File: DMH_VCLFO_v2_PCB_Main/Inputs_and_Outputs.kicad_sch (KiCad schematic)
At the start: 33 parts, among them J1 TS_Jack_6.35mm_Sw, J19 Conn_01x08, J2 TS_Jack_6.35mm_Sw, J200 IDC_02x05, J3 TS_Jack_6.35mm_Sw, J4 TS_Jack_6.35mm_Sw, J5 TS_Jack_6.35mm_Sw, J6 TS_Jack_6.35mm_Sw, J7 Conn_01x08, J8 Conn_01x08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

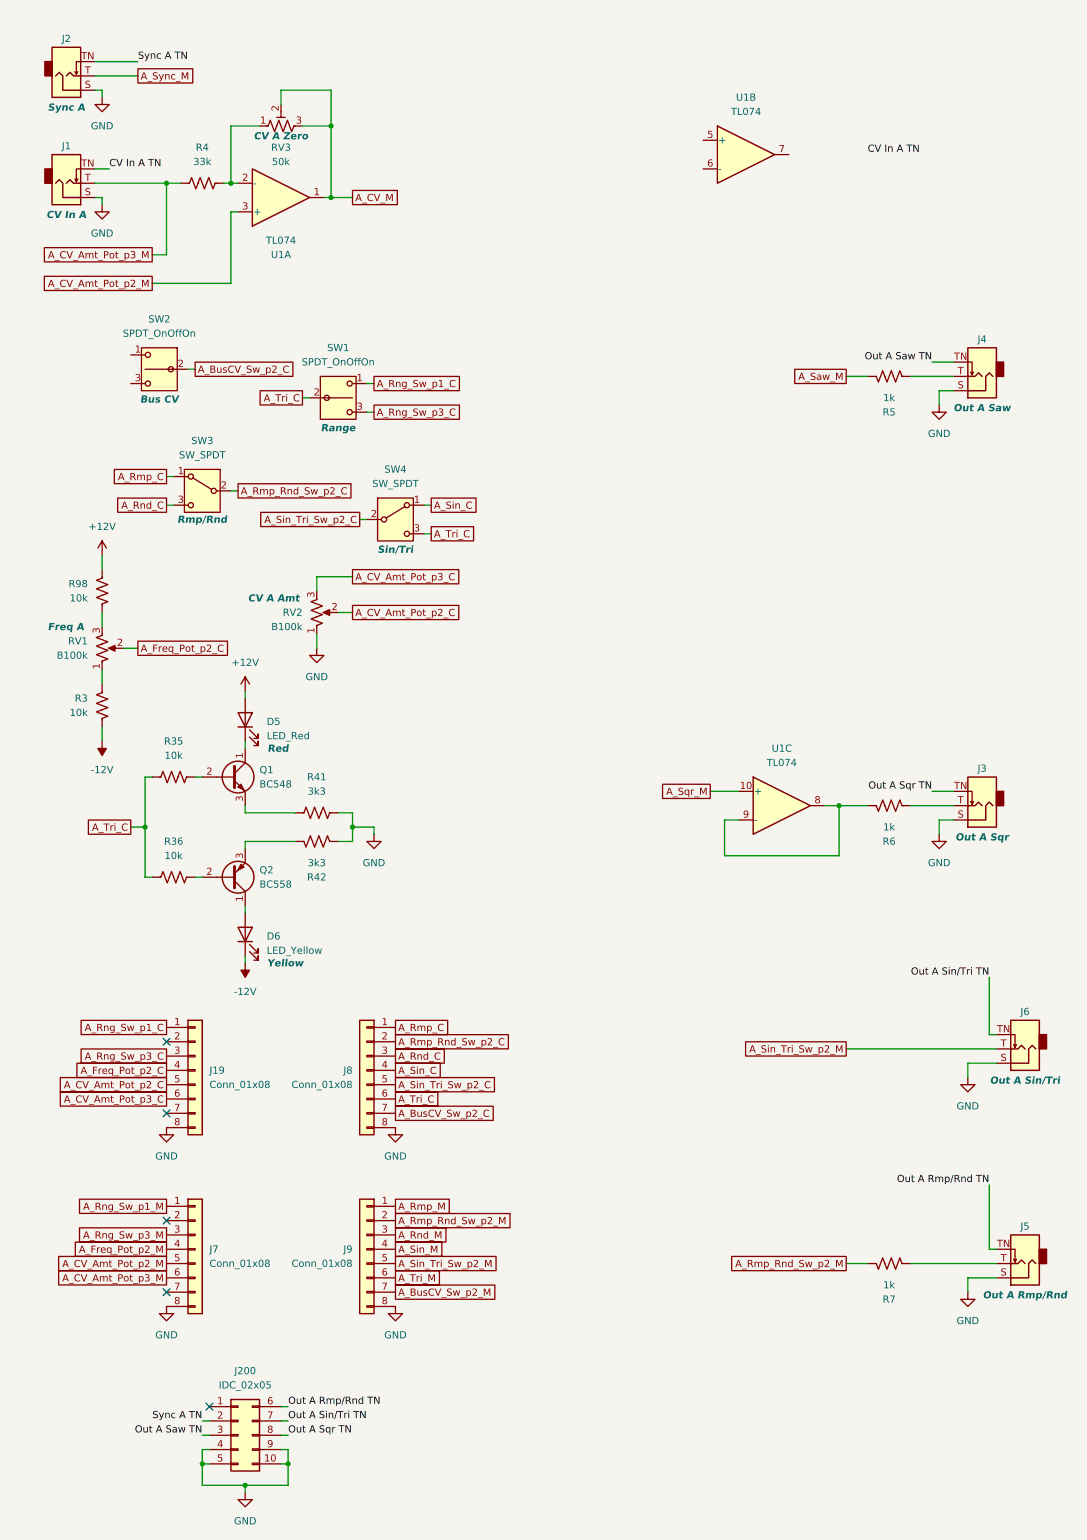
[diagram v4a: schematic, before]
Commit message: Redesigned schematic for V/Oct
And also Bus CV and Fine tune
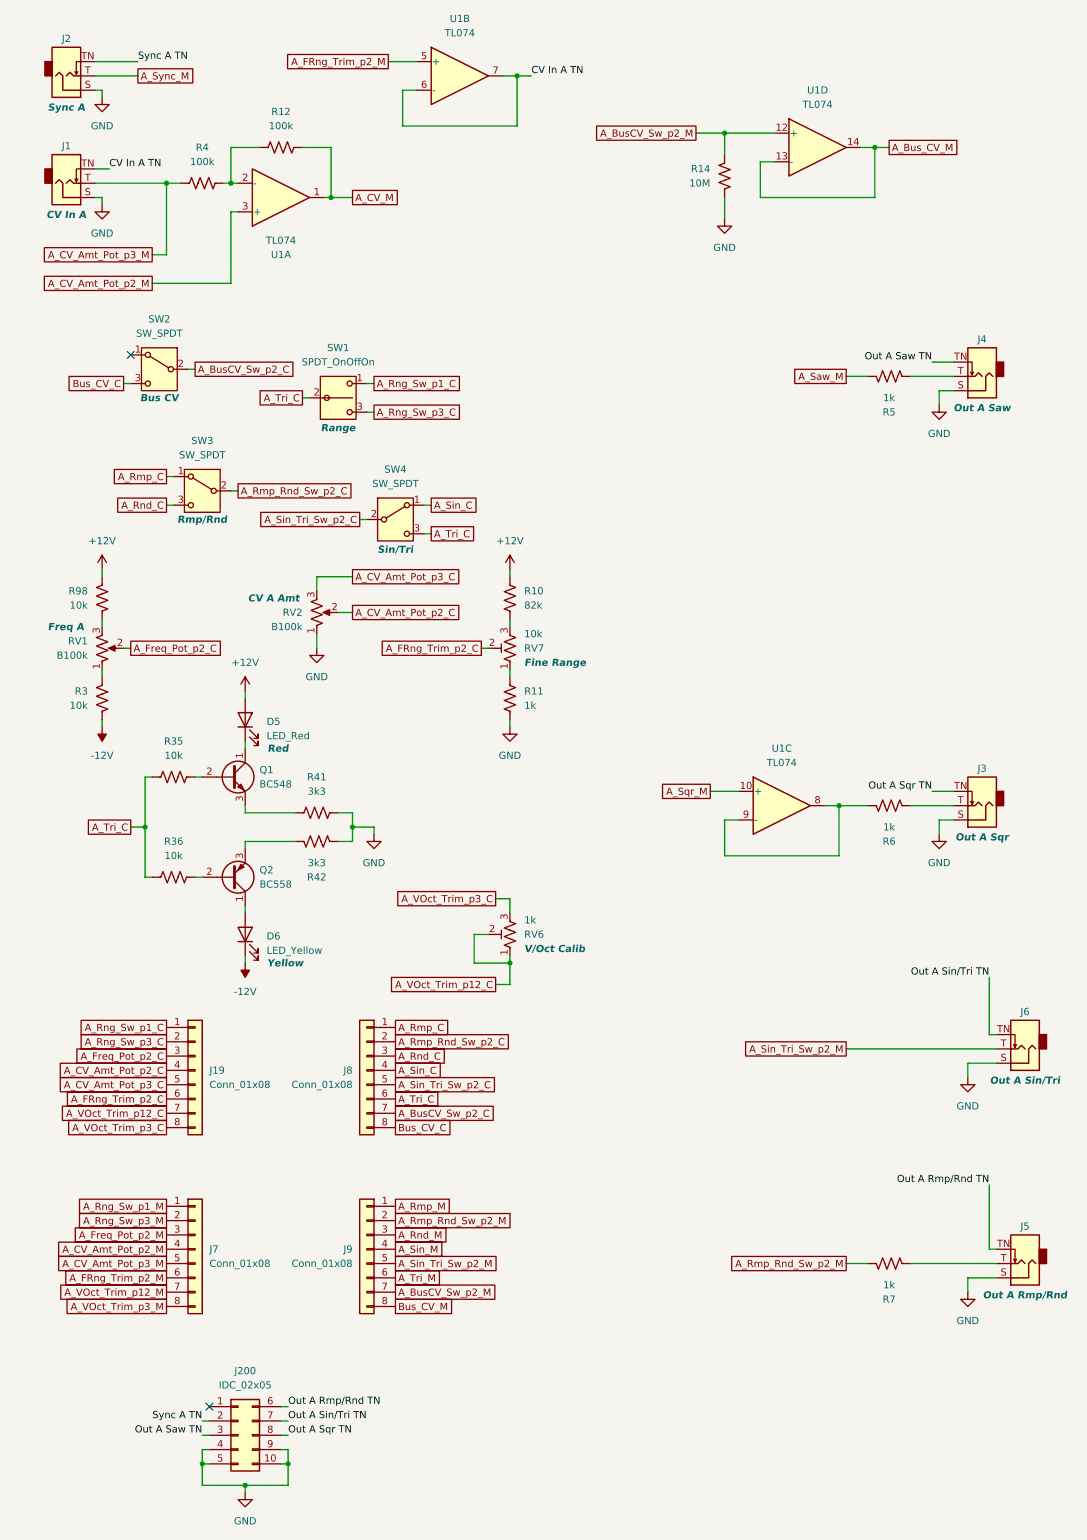
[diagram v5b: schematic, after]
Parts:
- removed RV3: 50k, Potentiometer_THT:Potentiometer_Bourns_3296X_Horizontal, symbol Device:R_Potentiometer_Trim_US
- removed SW2: SPDT_OnOffOn, SynthStuff:Toggle_Switch_TE, symbol SynthStuff:SW_SPDT_OnOffOn
- added R10: 82k, Resistor_THT:R_Axial_DIN0207_L6.3mm_D2.5mm_P7.62mm_Horizontal, symbol Device:R_US
- added R11: 1k, Resistor_THT:R_Axial_DIN0207_L6.3mm_D2.5mm_P7.62mm_Horizontal, symbol Device:R_US
- added R12: 100k, Resistor_THT:R_Axial_DIN0207_L6.3mm_D2.5mm_P7.62mm_Horizontal, symbol Device:R_US
- added R14: 10M, Resistor_THT:R_Axial_DIN0207_L6.3mm_D2.5mm_P7.62mm_Horizontal, symbol Device:R_US
- added RV6: 1k, Potentiometer_THT:Potentiometer_Bourns_3296W_Vertical, symbol Device:R_Potentiometer_Trim_US
- added RV7: 10k, Potentiometer_THT:Potentiometer_Bourns_3296W_Vertical, symbol Device:R_Potentiometer_Trim_US
- added SW2: SW_SPDT, SynthStuff:Toggle_Switch_TE, symbol Switch:SW_SPDT
- added unit 4 of U1
- R4: value 33k -> 100k
- U1: footprint Package_DIP:DIP-14_W7.62mm_Socket -> (none)
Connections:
- net +12V: now also R10.2
- net A_BusCV_Sw_p2_C: now also SW2.2 (B)
- net A_BusCV_Sw_p2_M: now also R14.1, U1.12 (+)
- net A_CV_Amt_Pot_p2_C: now also J19.4 (Pin_4); no longer J19.5 (Pin_5)
- net A_CV_Amt_Pot_p2_M: now also J7.4 (Pin_4); no longer J7.5 (Pin_5)
- net A_CV_Amt_Pot_p3_C: now also J19.5 (Pin_5); no longer J19.6 (Pin_6)
- net A_CV_Amt_Pot_p3_M: now also J7.5 (Pin_5); no longer J7.6 (Pin_6)
- net A_CV_M: now also R12.2
- net A_Freq_Pot_p2_C: now also J19.3 (Pin_3); no longer J19.4 (Pin_4)
- net A_Freq_Pot_p2_M: now also J7.3 (Pin_3); no longer J7.4 (Pin_4)
- net A_Rng_Sw_p3_C: now also J19.2 (Pin_2); no longer J19.3 (Pin_3)
- net A_Rng_Sw_p3_M: now also J7.2 (Pin_2); no longer J7.3 (Pin_3)
- net CV In A TN: now also U1.6 (-), U1.7
- net GND: now also R11.1, R14.2; no longer J19.8 (Pin_8), J7.8 (Pin_8), J8.8 (Pin_8), J9.8 (Pin_8)
- net at R4.2, U1.2 (-): now also R12.1
- net A_VOct_Trim_p12_M: now reaches J7.7 (Pin_7)
- net A_VOct_Trim_p12_C: now reaches J19.7 (Pin_7)
- net A_VOct_Trim_p12_C: now also RV6.1, RV6.2
- net A_FRng_Trim_p2_M: now reaches U1.5 (+)
- net A_FRng_Trim_p2_M: now also J7.6 (Pin_6)
- new net: R10.1, RV7.3
- new net: R11.2, RV7.1
- new net A_Bus_CV_M: U1.13 (-), U1.14
- new net A_FRng_Trim_p2_C: J19.6 (Pin_6), RV7.2
- new net A_VOct_Trim_p3_C: J19.8 (Pin_8), RV6.3
- new net A_VOct_Trim_p3_M: J7.8 (Pin_8)
- new net Bus_CV_C: J8.8 (Pin_8), SW2.3 (C)
- new net Bus_CV_M: J9.8 (Pin_8)
- no-connect marks 5 -> 2
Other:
- moved on the sheet: R3, R98, U1B
